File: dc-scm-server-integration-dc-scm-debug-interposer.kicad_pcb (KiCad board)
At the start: 6 copper layers, 90 x 40 mm, 208 parts, among them J1 Socket_DC-SCM-2.1_2x84_Rev-1-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, J10 PinHeader_2x5_P1.27mm_SMD, J11 PinHeader_2x5_P1.27mm_SMD, J12 PinHeader_2x5_P1.27mm_SMD, J13 PinHeader_2x5_P1.27mm_SMD, J14 PinHeader_2x5_P1.27mm_SMD_Shr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, J15 Socket_SOP2-16_ACA-SPI-006-K0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, J16 Socket_SOP2-16_ACA-SPI-006-K0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, J2 PCB-Edge_DC-SCM-2.1_2x84_Rev-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, J3 PinHeader_2x5_P1.27mm_SMD, J4 PinHeader_2x5_P1.27mm_SMD, J5 PinHeader_2x5_P1.27mm_SMD, J6 PinHeader_2x5_P1.27mm_SMD, J7 PinHeader_2x5_P1.27mm_SMD, J8 PinHeader_2x10_P1.27mm_SMD_Sh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, J9 PinHeader_2x5_P1.27mm_SMD, Q1 DMG1012T-7, Q2 DMG1012T-7, Q3 DMG1012T-7, U1 TLV76701_WSON

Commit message: [#100720] Continue placement of 0R
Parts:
- R1, R10, R106, R107, R110, R111, R114, R115, R118, R119, R12, R4, R49, R5, R50, R51, R52, R55, R6, R7, R8, R9, R99: moved to B.Cu
- moved R107 101.6 mm to (117.3, 78.0), turned to -90 degrees
- moved R106 100.5 mm to (118.4, 78.0), turned to -90 degrees
- moved R111 100.1 mm to (119.5, 80.0), turned to -90 degrees
- moved R115 99.9 mm to (121.6, 78.0), turned to -90 degrees
- moved R110 98.8 mm to (120.5, 80.0), turned to -90 degrees
- moved R114 98.4 mm to (122.6, 78.0), turned to -90 degrees
- moved R119 97.8 mm to (123.8, 80.0), turned to -90 degrees
- moved R118 96.8 mm to (124.8, 80.0), turned to -90 degrees
- moved R84 96.6 mm to (116.4, 87.7), turned to 90 degrees
- moved R85 94.7 mm to (118.4, 87.7), turned to 90 degrees
- moved R86 92.9 mm to (120.3, 87.7), turned to 90 degrees
- moved R87 91.1 mm to (122.3, 87.7), turned to 90 degrees
- moved R88 89.3 mm to (124.3, 87.7), turned to 90 degrees
- moved R89 87.7 mm to (126.3, 87.7), turned to 90 degrees
- moved R38 86.3 mm to (137.4, 94.2)
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
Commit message: [#100720] Finish placement of 0R
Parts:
- moved C1 202.0 mm to (152.1, 140.3)
- moved C2 202.0 mm to (152.1, 142.2)
- moved C3 202.0 mm to (152.1, 144.2)
- moved C4 202.0 mm to (152.1, 146.2)
- moved FD5 202.0 mm to (159.4, 153.0)
- moved FD6 202.0 mm to (159.4, 156.5)
- moved FD7 202.0 mm to (163.0, 153.0)
- moved FD8 202.0 mm to (163.0, 156.5)
- moved J16 202.0 mm to (174.1, 130.8)
- moved R131 202.0 mm to (152.1, 148.2)
- moved R134 202.0 mm to (158.2, 144.0)
- moved D1 202.0 mm to (145.6, 142.9)
- moved D2 202.0 mm to (145.6, 144.9)
- moved D3 202.0 mm to (161.8, 140.3)
- moved FD1 202.0 mm to (152.4, 153.0)
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
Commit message: [#100720] Place connectors
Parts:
- removed D1, D2: LED_G_0402_VLMTG1500-GS08, antmicro-footprints:LED_0402_1005Metric_G
- removed J14: PinHeader_2x5_P1.27mm_SMD_Shrouded, antmicro-footprints:PinHeader_2x5_P1.27mm_SMD_Shrouded
- removed J8: PinHeader_2x10_P1.27mm_SMD_Shrouded, antmicro-footprints:PinHeader_2x10_P1.27mm_SMD_Shrouded
- removed Q1, Q2: DMG1012T-7, antmicro-footprints:SOT-523
- removed R128, R130: R_10k_0402, antmicro-footprints:R_0402_1005Metric
- removed R129: R_100k_0402, antmicro-footprints:R_0402_1005Metric
- removed TP1, TP10, TP11, TP12, TP13, TP14, TP15, TP16, TP17, TP18, TP19, TP2, TP20, TP21, TP22, TP23, TP24, TP25, TP26, TP27, TP28, TP29, TP3, TP30, TP31, TP32, TP33, TP34, TP35, TP36, TP4, TP5, TP6, TP7, TP8, TP9: TP_1mm_SMD, antmicro-footprints:TP_SMD_1mm
- added J17: PinHeader_2x5_P2.54mm_SMD, antmicro-footprints:PinHeader_2x5_P2.54mm_SMD, F.Cu at (123.0, 102.7)
- J10, J11, J12, J13, J3, J4, J5, J6, J7, J9: value PinHeader_2x5_P1.27mm_SMD -> PinHeader_2x5_P2.54mm_SMD; footprint antmicro-footprints:PinHeader_2x5_P1.27mm_SMD -> antmicro-footprints:PinHeader_2x5_P2.54mm_SMD
- moved FD1 121.5 mm to (115.5, 37.2)
- moved FD2 121.5 mm to (115.5, 40.7)
- moved FD3 121.5 mm to (119.0, 37.2)
- moved FD4 121.5 mm to (119.0, 40.7)
- moved FD5 121.5 mm to (122.5, 37.2)
- moved FD6 121.5 mm to (122.5, 40.7)
- moved FD7 121.5 mm to (126.0, 37.2)
- moved FD8 121.5 mm to (126.0, 40.7)
- moved C1 102.4 mm to (76.4, 71.2)
- moved C2 102.4 mm to (76.4, 73.2)
- moved C3 102.4 mm to (76.4, 75.2)
- moved C4 102.4 mm to (76.4, 77.2)
- moved R131 102.4 mm to (76.4, 79.2)
- moved R133 102.4 mm to (79.3, 73.2)
- moved R134 102.4 mm to (82.5, 74.9)
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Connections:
- J12 pad 8: +1V8 -> GND
- J13 pad 1: /DC-SCI edge connector/DC_SCM_12V_AUX -> /DC-SCI edge connector/DC_SCM_JTAG.TMS
- J13 pad 10: /DC-SCI edge connector/~{DC_SCM_SPI_SCMCNTRL_IRQ0} -> /DC-SCI edge connector/~{DC_SCM_INTRUSION}
- J13 pad 3: /DC-SCI edge connector/DC_SCM_P3V0 -> /DC-SCI edge connector/DC_SCM_JTAG.TCK
- J13 pad 5: /DC-SCI edge connector/DC_SCM_PRSNT0_N -> /DC-SCI edge connector/DC_SCM_JTAG.TDO
- J13 pad 6: /DC-SCI edge connector/DC_SCM_HPM_FRU -> /DC-SCI edge connector/DC_SCM_PRSNT0_N
- J13 pad 7: /DC-SCI edge connector/DC_SCM_PRSNT1_N -> /DC-SCI edge connector/DC_SCM_JTAG.TDI
- J13 pad 8: /DC-SCI edge connector/PECI_VREF_HPM_SCM -> /DC-SCI edge connector/DC_SCM_PRSNT1_N
- J13 pad 9: /DC-SCI edge connector/~{DC_SCM_INTRUSION} -> /DC-SCI edge connector/DC_SCM_JTAG.TRST
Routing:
- net /DC-SCI edge connector/DC_SCM_I2C_I3C14.SCL: track 0.00 -> 27.9 mm
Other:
- board size 90 x 40 mm -> 90 x 69.9 mm

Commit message: [#100720] Finish placement
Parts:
- removed R134: R_0R_22.4A_0603, antmicro-footprints:R_0603_1608Metric
- added R128: R_0R_0402, antmicro-footprints:R_0402_1005Metric, F.Cu at (108.9, 105.4)
- FD5, FD6, FD7, FD8, R13, R2, R3: moved to B.Cu
- R100, R101, R102, R103, R106, R107, R110, R111, R114, R115, R118, R119, R122, R123, R124, R125, R49, R50, R51, R52: moved to F.Cu
- moved FD3 112.5 mm to (187.5, 126.4)
- moved FD7 108.3 mm to (187.5, 126.4), turned to 180 degrees
- moved FD8 88.9 mm to (102.5, 126.4), turned to 180 degrees
- moved FD4 87.3 mm to (102.5, 126.4)
- moved FD2 80.2 mm to (187.5, 76.0)
- moved FD6 73.9 mm to (187.5, 76.0), turned to 180 degrees
- moved C3 62.7 mm to (129.6, 108.4)
- moved R136 58.6 mm to (129.6, 107.3)
- moved C4 47.8 mm to (112.6, 108.4)
- moved R132 43.7 mm to (108.9, 103.4)
- moved FD5 43.7 mm to (102.5, 76.0), turned to 180 degrees
- moved R137 43.6 mm to (112.6, 107.3)
- moved C2 43.0 mm to (108.9, 101.4), turned to 180 degrees
- moved R133 43.0 mm to (108.9, 104.4), turned to 180 degrees
- moved C1 41.0 mm to (108.9, 96.2), turned to 180 degrees
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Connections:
- J7 pad 10: GND -> /DC-SCI edge connector/DC_SCM_I2C_I3C19.SCL
- J7 pad 3: /DC-SCI edge connector/DC_SCM_I2C_I3C18.SCL -> GND
- J7 pad 6: GND -> /DC-SCI edge connector/DC_SCM_I2C_I3C18.SCL
- J7 pad 7: /DC-SCI edge connector/DC_SCM_I2C_I3C19.SCL -> GND
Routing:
- net /DC-SCI edge connector/DC_SCM_I2C_I3C14.SCL: track 27.9 -> 3.18 mm
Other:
- board size 90 x 69.9 mm -> 90 x 62.3 mm

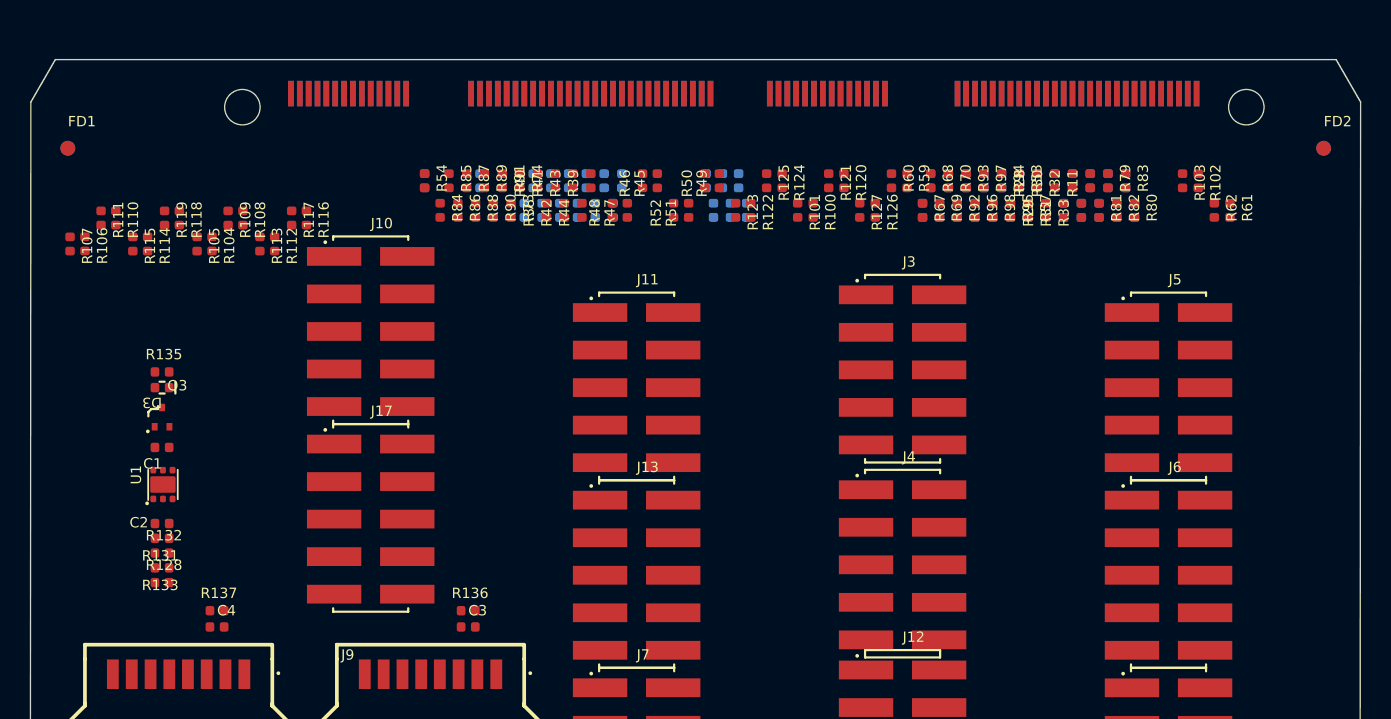
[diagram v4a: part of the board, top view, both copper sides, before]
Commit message: [#100720] Start routing high speeds
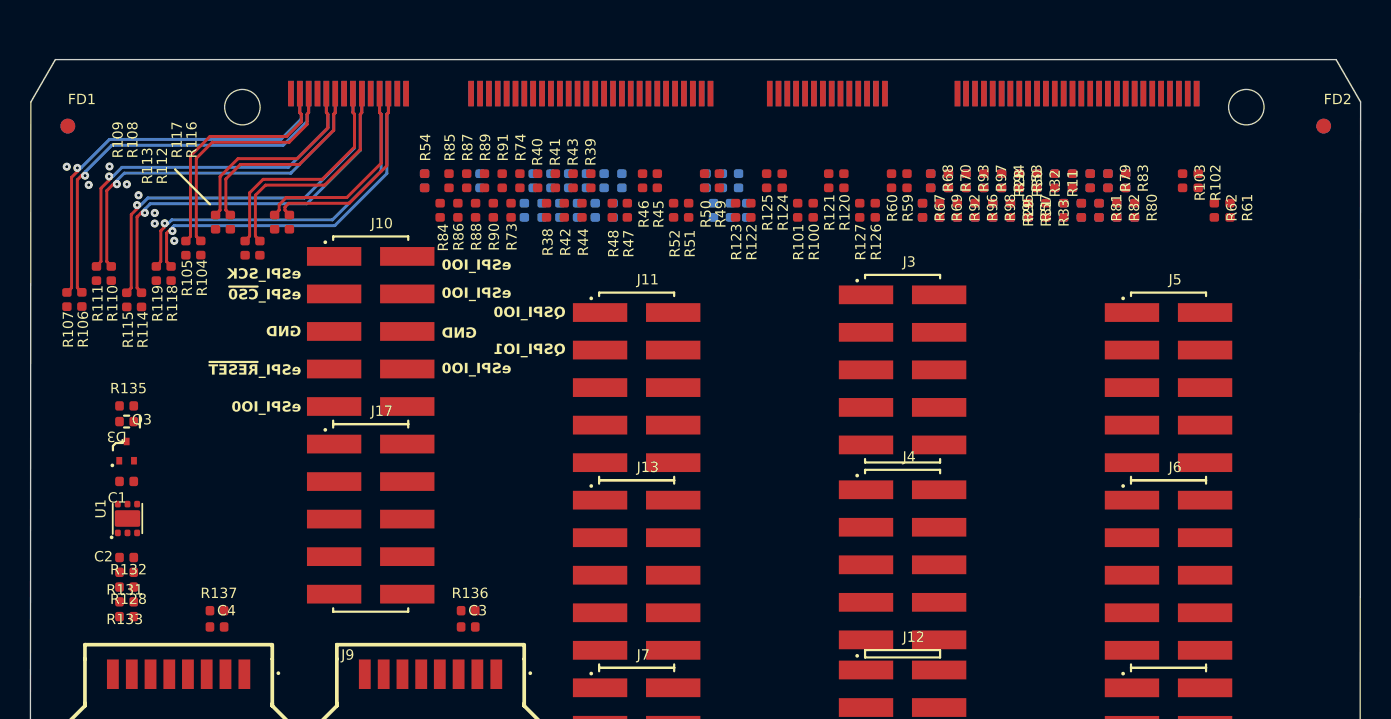
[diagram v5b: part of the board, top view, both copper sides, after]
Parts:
- moved R114 3.80 mm to (107.5, 86.3)
- moved R115 3.80 mm to (106.5, 86.3)
- moved R118 3.80 mm to (109.5, 84.5)
- moved R119 3.80 mm to (108.5, 84.5)
- moved R110 3.77 mm to (105.4, 84.5)
- moved R111 3.77 mm to (104.4, 84.5)
- moved R107 3.77 mm to (102.4, 86.2)
- moved R106 3.77 mm to (103.5, 86.2)
- moved C1 3.32 mm to (106.5, 98.5)
- moved C2 3.32 mm to (106.5, 103.7)
- moved D3 3.32 mm to (106.5, 94.5)
- moved Q3 3.32 mm to (106.5, 96.5)
- moved R128 3.32 mm to (106.5, 107.7)
- moved R131 3.32 mm to (106.5, 104.7)
- moved R132 3.32 mm to (106.5, 105.7)
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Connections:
- net Net-(J1D-PCIE_HPMROOT_HPM_SCM_0_DN) renamed /DC-SCI gold fingers connector/PCIE0_SGMII_TX0-
- net Net-(J1D-PCIE_HPMROOT_HPM_SCM_0_DP) renamed /DC-SCI gold fingers connector/PCIE0_SGMII_TX0+
- net Net-(J1D-PCIE_HPMROOT_HPM_SCM_1_DN) renamed /DC-SCI gold fingers connector/PCIE0_SGMII_TX1-
- net Net-(J1D-PCIE_HPMROOT_HPM_SCM_1_DP) renamed /DC-SCI gold fingers connector/PCIE0_SGMII_TX1+
- net Net-(J1D-PCIE_HPMROOT_HPM_SCM_2_DN) renamed /DC-SCI gold fingers connector/PCIE0_SGMII_TX2-
- net Net-(J1D-PCIE_HPMROOT_HPM_SCM_2_DP) renamed /DC-SCI gold fingers connector/PCIE0_SGMII_TX2+
- net Net-(J1D-PCIE_HPMROOT_HPM_SCM_3_DN) renamed /DC-SCI gold fingers connector/PCIE0_SGMII_TX3-
- net Net-(J1D-PCIE_HPMROOT_HPM_SCM_3_DP) renamed /DC-SCI gold fingers connector/PCIE0_SGMII_TX3+
- net Net-(J1D-PCIE_HPMROOT_HPM_SCM_4_DN) renamed /DC-SCI gold fingers connector/PCIE1_TX0-
- net Net-(J1D-PCIE_HPMROOT_HPM_SCM_4_DP) renamed /DC-SCI gold fingers connector/PCIE1_TX0+
- net Net-(J1D-PCIE_HPMROOT_SCM_HPM_0_DN) renamed /DC-SCI gold fingers connector/PCIE0_SGMII_RX0-
- net Net-(J1D-PCIE_HPMROOT_SCM_HPM_0_DP) renamed /DC-SCI gold fingers connector/PCIE0_SGMII_RX0+
- net Net-(J1D-PCIE_HPMROOT_SCM_HPM_1_DN) renamed /DC-SCI gold fingers connector/PCIE0_SGMII_RX1-
- net Net-(J1D-PCIE_HPMROOT_SCM_HPM_1_DP) renamed /DC-SCI gold fingers connector/PCIE0_SGMII_RX1+
- net Net-(J1D-PCIE_HPMROOT_SCM_HPM_2_DN) renamed /DC-SCI gold fingers connector/PCIE0_SGMII_RX2-
- net Net-(J1D-PCIE_HPMROOT_SCM_HPM_2_DP) renamed /DC-SCI gold fingers connector/PCIE0_SGMII_RX2+
- net Net-(J1D-PCIE_HPMROOT_SCM_HPM_3_DN) renamed /DC-SCI gold fingers connector/PCIE0_SGMII_RX3-
- net Net-(J1D-PCIE_HPMROOT_SCM_HPM_3_DP) renamed /DC-SCI gold fingers connector/PCIE0_SGMII_RX3+
- net Net-(J1D-PCIE_HPMROOT_SCM_HPM_4_DN) renamed /DC-SCI gold fingers connector/PCIE1_RX0-
- net Net-(J1D-PCIE_HPMROOT_SCM_HPM_4_DP) renamed /DC-SCI gold fingers connector/PCIE1_RX0+
- net Net-(J1D-PCIE_HPM_SCM_CLK_100M_0_DN) renamed /DC-SCI gold fingers connector/CLK_100M_0_CLK-
- net Net-(J1D-PCIE_HPM_SCM_CLK_100M_0_DP) renamed /DC-SCI gold fingers connector/CLK_100M_0_CLK+
- net Net-(J1D-PCIE_SCMROOT_HPM_SCM_DN) renamed /DC-SCI gold fingers connector/PCIE_USB_SCMROOT_TX0-
- net Net-(J1D-PCIE_SCMROOT_HPM_SCM_DP) renamed /DC-SCI gold fingers connector/PCIE_USB_SCMROOT_TX0+
- net Net-(J1D-PCIE_SCMROOT_SCM_HPM_DN) renamed /DC-SCI gold fingers connector/PCIE_USB_SCMROOT_RX0-
- net Net-(J1D-PCIE_SCMROOT_SCM_HPM_DP) renamed /DC-SCI gold fingers connector/PCIE_USB_SCMROOT_RX0+
- J1 pad A68: Net-(J1D-PCIE_HPM_SCM_CLK_100M_1_S0_DN) -> /DC-SCI gold fingers connector/CLK_100M_1_CLK+
- J1 pad A69: Net-(J1D-PCIE_HPM_SCM_CLK_100M_1_S0_DP) -> /DC-SCI gold fingers connector/CLK_100M_1_CLK+
- R102 pad 1: Net-(J1D-PCIE_HPM_SCM_CLK_100M_1_S0_DP) -> /DC-SCI gold fingers connector/CLK_100M_1_CLK+
- R103 pad 1: Net-(J1D-PCIE_HPM_SCM_CLK_100M_1_S0_DN) -> /DC-SCI gold fingers connector/CLK_100M_1_CLK+
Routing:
- net /DC-SCI gold fingers connector/PCIE0_SGMII_RX0-: track 0.00 -> 27.0 mm, vias 0 -> 1
- net /DC-SCI gold fingers connector/PCIE0_SGMII_RX0+: track 0.00 -> 27.0 mm, vias 0 -> 1
- net /DC-SCI gold fingers connector/PCIE0_SGMII_RX2-: track 0.00 -> 26.3 mm, vias 0 -> 1
- net /DC-SCI gold fingers connector/PCIE0_SGMII_RX2+: track 0.00 -> 26.3 mm, vias 0 -> 1
- net /DC-SCI gold fingers connector/PCIE0_SGMII_RX1+: track 0.00 -> 25.0 mm, vias 0 -> 1
- net /DC-SCI gold fingers connector/PCIE0_SGMII_RX1-: track 0.00 -> 25.0 mm, vias 0 -> 1
- net /DC-SCI gold fingers connector/PCIE0_SGMII_RX3-: track 0.00 -> 24.6 mm, vias 0 -> 1
- net /DC-SCI gold fingers connector/PCIE0_SGMII_RX3+: track 0.00 -> 24.6 mm, vias 0 -> 1
- net /DC-SCI gold fingers connector/PCIE0_SGMII_TX0-: track 0.00 -> 16.3 mm
- net /DC-SCI gold fingers connector/PCIE0_SGMII_TX0+: track 0.00 -> 16.3 mm
- net /DC-SCI gold fingers connector/PCIE0_SGMII_TX2+: track 0.00 -> 15.4 mm
- net /DC-SCI gold fingers connector/PCIE0_SGMII_TX2-: track 0.00 -> 15.4 mm
- net /DC-SCI gold fingers connector/PCIE0_SGMII_TX1-: track 0.00 -> 13.8 mm
- net /DC-SCI gold fingers connector/PCIE0_SGMII_TX1+: track 0.00 -> 13.8 mm
- net /DC-SCI gold fingers connector/PCIE0_SGMII_TX3+: track 0.00 -> 13.6 mm
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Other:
- board text added: "GND"
- board text added: "QSPI_IO0"
- board text added: "QSPI_IO1"
- board text added: "eSPI_IO0"
- board text added: "eSPI_SCK"
- board text added: "eSPI_~{CS0}"
- board text added: "eSPI_~{RESET}"
